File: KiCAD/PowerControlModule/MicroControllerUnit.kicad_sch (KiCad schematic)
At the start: 3 parts, among them U1 XIAO-RP2040-DIP

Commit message: PowerControlModuleを作成．ソフトウェアの開発も進めなければいけない....
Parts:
- renumbered R22 to R1, R23 to R2
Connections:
- net GPU_ENSW renamed VREF_T1
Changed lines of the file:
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@@
+		)
+	)
+	(global_label "VREF_T1"
+		(shape input)
+		(at 96.52 44.45 180)
+		(fields_autoplaced yes)
+		(effects
+			(font
+				(size 1.27 1.27)
+			)
+			(justify right)
+		)
+		(property "Intersheetrefs" "${INTERSHEET_REFS}"
+			(at 85.7939 44.45 0)
+			(effects
+				(font
+					(size 1.27 1.27)
+				)
+				(justify right)
+				(hide yes)
+			)
 		)
 	)
@@
 		(property "Intersheetrefs" "${INTERSHEET_REFS}"
 			(at 80.714 40.64 0)
-			(effects
-				(font
-					(size 1.27 1.27)
-				)
-				(justify right)
-				(hide yes)
-			)
-		)
-	)
-	(global_label "GPU_ENSW"
-		(shape input)
-		(at 96.52 44.45 180)
-		(fields_autoplaced yes)
-		(effects
-			(font
-				(size 1.27 1.27)
-			)
-			(justify right)
-		)
-		(property "Intersheetrefs" "${INTERSHEET_REFS}"
-			(at 83.5563 44.45 0)
 			(effects
 				(font
@@
 		(dnp no)
 		(fields_autoplaced yes)
-		(property "Reference" "#PWR049"
+		(property "Reference" "#PWR01"
 			(at 52.07 45.72 0)
 			(effects
@@
 			(project "PowerControlModule"
 				(path "/cd54ca1c-60d1-49a2-85aa-1c2ce8b76912/b3d71d1b-7a87-43b2-b3d1-d977f5dcfe8c"
-					(reference "#PWR049")
+					(reference "#PWR01")
 					(unit 1)
 				)
@@
 		(dnp no)
 		(fields_autoplaced yes)
-		(property "Reference" "R23"
+		(property "Reference" "R2"
 			(at 66.04 45.7199 0)
 			(effects
@@
 			(project "PowerControlModule"
 				(path "/cd54ca1c-60d1-49a2-85aa-1c2ce8b76912/b3d71d1b-7a87-43b2-b3d1-d977f5dcfe8c"
-					(reference "R23")
+					(reference "R2")
 					(unit 1)
 				)
@@
 		(dnp no)
 		(fields_autoplaced yes)
-		(property "Reference" "#PWR03"
+		(property "Reference" "#PWR05"
 			(at 149.86 48.26 0)
 			(effects
@@
 			(project ""
 				(path "/cd54ca1c-60d1-49a2-85aa-1c2ce8b76912/b3d71d1b-7a87-43b2-b3d1-d977f5dcfe8c"
-					(reference "#PWR03")
+					(reference "#PWR05")
 					(unit 1)
 				)
@@
 		(dnp no)
 		(fields_autoplaced yes)
-		(property "Reference" "#PWR02"
+		(property "Reference" "#PWR04"
 			(at 130.81 44.45 0)
 			(effects
@@
 			(project ""
 				(path "/cd54ca1c-60d1-49a2-85aa-1c2ce8b76912/b3d71d1b-7a87-43b2-b3d1-d977f5dcfe8c"
-					(reference "#PWR02")
+					(reference "#PWR04")
 					(unit 1)
 				)
@@
 		(dnp no)
 		(fields_autoplaced yes)
-		(property "Reference" "R22"
+		(property "Reference" "R1"
 			(at 54.61 45.7199 0)
 			(effects
@@
 			(project ""
 				(path "/cd54ca1c-60d1-49a2-85aa-1c2ce8b76912/b3d71d1b-7a87-43b2-b3d1-d977f5dcfe8c"
-					(reference "R22")
+					(reference "R1")
 					(unit 1)
 				)
@@
 		(dnp no)
 		(fields_autoplaced yes)
-		(property "Reference" "#PWR050"
+		(property "Reference" "#PWR02"
 			(at 63.5 45.72 0)
 			(effects
@@
 			(project "PowerControlModule"
 				(path "/cd54ca1c-60d1-49a2-85aa-1c2ce8b76912/b3d71d1b-7a87-43b2-b3d1-d977f5dcfe8c"
-					(reference "#PWR050")
+					(reference "#PWR02")
 					(unit 1)
 				)
@@
 		(dnp no)
 		(fields_autoplaced yes)
-		(property "Reference" "#PWR01"
+		(property "Reference" "#PWR03"
 			(at 130.81 36.83 0)
 			(effects
@@
 			(project ""
 				(path "/cd54ca1c-60d1-49a2-85aa-1c2ce8b76912/b3d71d1b-7a87-43b2-b3d1-d977f5dcfe8c"
-					(reference "#PWR01")
+					(reference "#PWR03")
 					(unit 1)
 				)

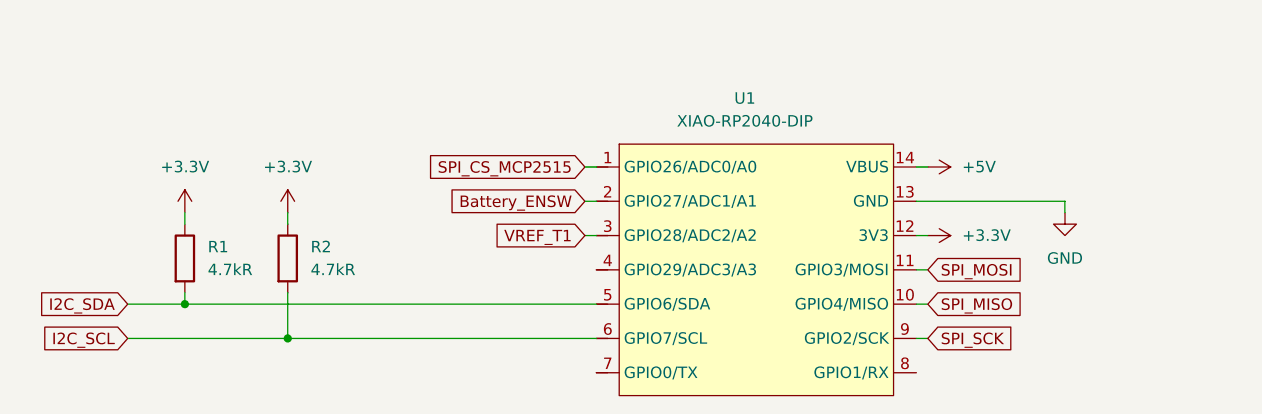
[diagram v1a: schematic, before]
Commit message: PowerModule，Build-2完成．発注．
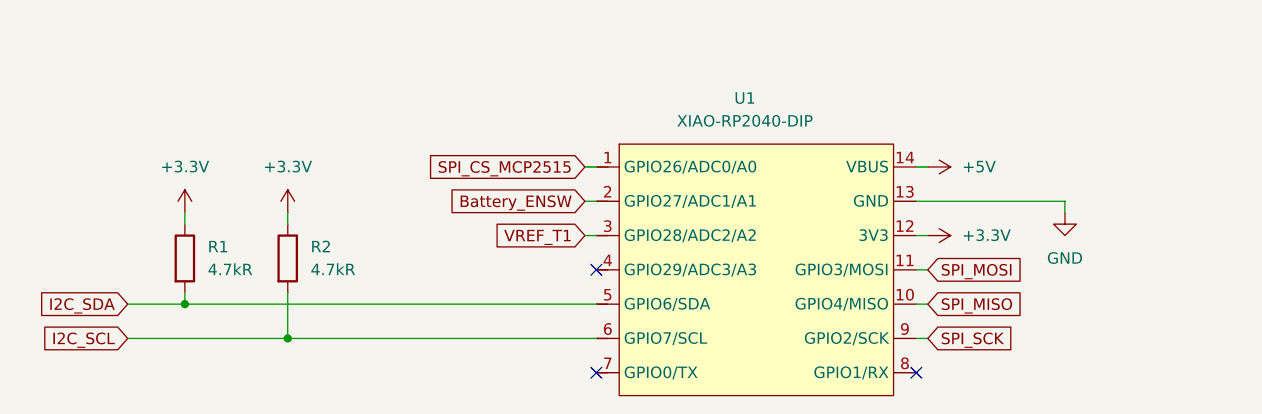
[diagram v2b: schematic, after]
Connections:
- no-connect marks 0 -> 3
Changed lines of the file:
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@@
 		(color 0 0 0 0)
+	)
+	(no_connect
+		(at 97.79 59.69)
+	)
+	(no_connect
+		(at 97.79 48.26)
+	)
+	(no_connect
+		(at 133.35 59.69)
 	)
 	(wire
@@
 			)
 		)
-		(property "Datasheet" ""
+		(property "Datasheet" "https://akizukidenshi.com/catalog/g/g117044/"
 			(at 100.33 31.75 0)
 			(effects

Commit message: Build-3完成．本日発注．
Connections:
- net Battery_ENSW is gone; now on net VREF_T1: U1.2 (GPIO27/ADC1/A1)
- net VREF_T1: no longer U1.3 (GPIO28/ADC2/A2)
- net LTC4353_EN2: now reaches U1.4 (GPIO29/ADC3/A3)
- net BATT_EN: now reaches U1.7 (GPIO0/TX)
- new net LTC4353_EN1: U1.3 (GPIO28/ADC2/A2)
- no-connect marks 3 -> 1
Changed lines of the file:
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@@
-	)
-	(no_connect
-		(at 97.79 59.69)
-	)
-	(no_connect
-		(at 97.79 48.26)
 	)
 	(no_connect
@@
 	(wire
 		(pts
+			(xy 96.52 59.69) (xy 97.79 59.69)
+		)
+		(stroke
+			(width 0)
+			(type default)
+		)
+	)
+	(wire
+		(pts
 			(xy 133.35 40.64) (xy 149.86 40.64)
 		)
@@
 	(wire
 		(pts
+			(xy 96.52 48.26) (xy 97.79 48.26)
+		)
+		(stroke
+			(width 0)
+			(type default)
+		)
+	)
+	(wire
+		(pts
 			(xy 63.5 41.91) (xy 63.5 43.18)
 		)
@@
 		)
 	)
-	(global_label "VREF_T1"
+	(global_label "BATT_EN"
 		(shape input)
-		(at 96.52 44.45 180)
+		(at 96.52 59.69 180)
 		(fields_autoplaced yes)
 		(effects
@@
 		)
 		(property "Intersheetrefs" "${INTERSHEET_REFS}"
-			(at 85.7939 44.45 0)
+			(at 85.7939 59.69 0)
+			(effects
+				(font
+					(size 1.27 1.27)
+				)
+				(justify right)
+				(hide yes)
+			)
+		)
+	)
+	(global_label "VREF_T1"
+		(shape input)
+		(at 96.52 40.64 180)
+		(fields_autoplaced yes)
+		(effects
+			(font
+				(size 1.27 1.27)
+			)
+			(justify right)
+		)
+		(property "Intersheetrefs" "${INTERSHEET_REFS}"
+			(at 85.7939 40.64 0)
 			(effects
 				(font
@@
 		)
 	)
+	(global_label "LTC4353_EN2"
+		(shape input)
+		(at 96.52 48.26 180)
+		(fields_autoplaced yes)
+		(effects
+			(font
+				(size 1.27 1.27)
+			)
+			(justify right)
+		)
+		(property "Intersheetrefs" "${INTERSHEET_REFS}"
+			(at 80.7745 48.26 0)
+			(effects
+				(font
+					(size 1.27 1.27)
+				)
+				(justify right)
+				(hide yes)
+			)
+		)
+	)
 	(global_label "SPI_SCK"
 		(shape input)
@@
 		)
 	)
-	(global_label "Battery_ENSW"
+	(global_label "LTC4353_EN1"
 		(shape input)
-		(at 96.52 40.64 180)
+		(at 96.52 44.45 180)
 		(fields_autoplaced yes)
 		(effects
@@
 		)
 		(property "Intersheetrefs" "${INTERSHEET_REFS}"
-			(at 80.714 40.64 0)
+			(at 80.7745 44.45 0)
 			(effects
 				(font
@@
 			)
 		)
+		(property "Sim.Type" ""
+			(at 63.5 46.99 0)
+			(effects
+				(font
+					(size 1.27 1.27)
+				)
+			)
+		)
 		(pin "1"
 		)
@@
 			)
 		)
+		(property "Sim.Type" ""
+			(at 52.07 46.99 0)
+			(effects
+				(font
+					(size 1.27 1.27)
+				)
+			)
+		)
 		(pin "1"
 		)
@@
 			)
 		)
+		(property "Sim.Type" ""
+			(at 100.33 31.75 0)
+			(effects
+				(font
+					(size 1.27 1.27)
+				)
+			)
+		)

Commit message: Build-5を作成
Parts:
- added D11: SS2040FL, Diode_SMD:D_SOD-123F, symbol Device:D_Schottky
- added R23: 4.7kR, Resistor_SMD:R_0603_1608Metric_Pad0.98x0.95mm_HandSolder, symbol Device:R
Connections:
- net +3.3V: now also R23.1
- net +5V: now also D11.2 (A); no longer U1.14 (VBUS)
- net SPI_CS_MCP2515: now also R23.2
- new net: D11.1 (K), U1.14 (VBUS)
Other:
- moved on the sheet: U1

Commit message: 修正した．発注する．
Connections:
- net LTC3119_PGOOD: now reaches U1.8 (GPIO1/RX)
- no-connect marks 1 -> 0
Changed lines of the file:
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@@
 		(color 0 0 0 0)
 	)
-	(no_connect
-		(at 146.05 59.69)
-	)
 	(wire
 		(pts
@@
 	(wire
 		(pts
+			(xy 146.05 59.69) (xy 147.32 59.69)
+		)
+		(stroke
+			(width 0)
+			(type default)
+		)
+	)
+	(wire
+		(pts
 			(xy 162.56 40.64) (xy 162.56 41.91)
 		)
@@
 			(effects
 				(font
+					(size 1.27 1.27)
+				)
+				(justify left)
+				(hide yes)
+			)
+		)
+	)
+	(global_label "LTC3119_PGOOD"
+		(shape input)
+		(at 147.32 59.69 0)
+		(fields_autoplaced yes)
+		(effects
+			(font
+				(size 1.27 1.27)
+			)
+			(justify left)
+		)
+		(property "Intersheetrefs" "${INTERSHEET_REFS}"
+			(at 165.8475 59.69 0)
+			(effects
+				(font
